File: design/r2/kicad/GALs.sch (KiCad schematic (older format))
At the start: 11 parts, among them IC10 ATF22V10C, IC2 ATF16V8BQL-15PU, IC3 ATF22V10C, IC5 ATF16V8BQL-15PU

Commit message: Tidy up footprints
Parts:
- C10, C12, C30: footprint Capacitor_THT:C_Rect_L4.0mm_W2.5mm_P2.50mm -> rosco_m68k:C2.5-3
- IC2, IC5: footprint rosco_m68k:DIL20 -> Package_DIP:DIP-24_W7.62mm_Socket_LongPads
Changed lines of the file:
@@
 $Descr A4 11693 8268
 encoding utf-8
-Sheet 8 7
+Sheet 7 7
 Title "rosco_m68k Pro (030) Prototype"
 Date "2021-10-01"
@@
 F 0 "C12" H 5910 3715 59  0000 L BNN
 F 1 "100nF" H 5910 3515 59  0000 L BNN
-F 2 "Capacitor_THT:C_Rect_L4.0mm_W2.5mm_P2.50mm" H 5850 3700 50  0001 C CNN
+F 2 "rosco_m68k:C2.5-3" H 5850 3700 50  0001 C CNN
 F 3 "" H 5850 3700 50  0001 C CNN
 	1    5850 3700
@@
 F 0 "C31" H 8060 3715 59  0000 L BNN
 F 1 "100nF" H 8060 3515 59  0000 L BNN
-F 2 "Capacitor_THT:C_Rect_L4.0mm_W2.5mm_P2.50mm" H 8000 3700 50  0001 C CNN
+F 2 "rosco_m68k:C2.5-3" H 8000 3700 50  0001 C CNN
 F 3 "" H 8000 3700 50  0001 C CNN
 	1    8000 3700
@@
 F 0 "IC5" H 6950 4786 59  0000 C CNN
 F 1 "ATF16V8BQL-15PU" H 6950 4681 59  0000 C CNN
-F 2 "rosco_m68k:DIL20" H 6950 3900 50  0001 C CNN
-F 3 "" H 6950 3900 50  0001 C CNN
+F 2 "Package_DIP:DIP-24_W7.62mm_Socket_LongPads" H 6950 3900 50  0001 C CNN
+F 3 "https://www.mouser.com/datasheet/2/268/doc0735-1369018.pdf" H 6950 3900 50  0001 C CNN
 	1    6950 3900
 	1    0    0    -1
@@
 F 0 "IC2" H 2500 4786 59  0000 C CNN
 F 1 "ATF16V8BQL-15PU" H 2500 4681 59  0000 C CNN
-F 2 "rosco_m68k:DIL20" H 2500 3900 50  0001 C CNN
-F 3 "" H 2500 3900 50  0001 C CNN
+F 2 "Package_DIP:DIP-24_W7.62mm_Socket_LongPads" H 2500 3900 50  0001 C CNN
+F 3 "https://www.mouser.com/datasheet/2/268/doc0735-1369018.pdf" H 2500 3900 50  0001 C CNN
 	1    2500 3900
 	1    0    0    -1
@@
 F 0 "C10" H 10360 3715 59  0000 L BNN
 F 1 "100nF" H 10360 3515 59  0000 L BNN
-F 2 "Capacitor_THT:C_Rect_L4.0mm_W2.5mm_P2.50mm" H 10300 3700 50  0001 C CNN
+F 2 "rosco_m68k:C2.5-3" H 10300 3700 50  0001 C CNN
 F 3 "" H 10300 3700 50  0001 C CNN
 	1    10300 3700

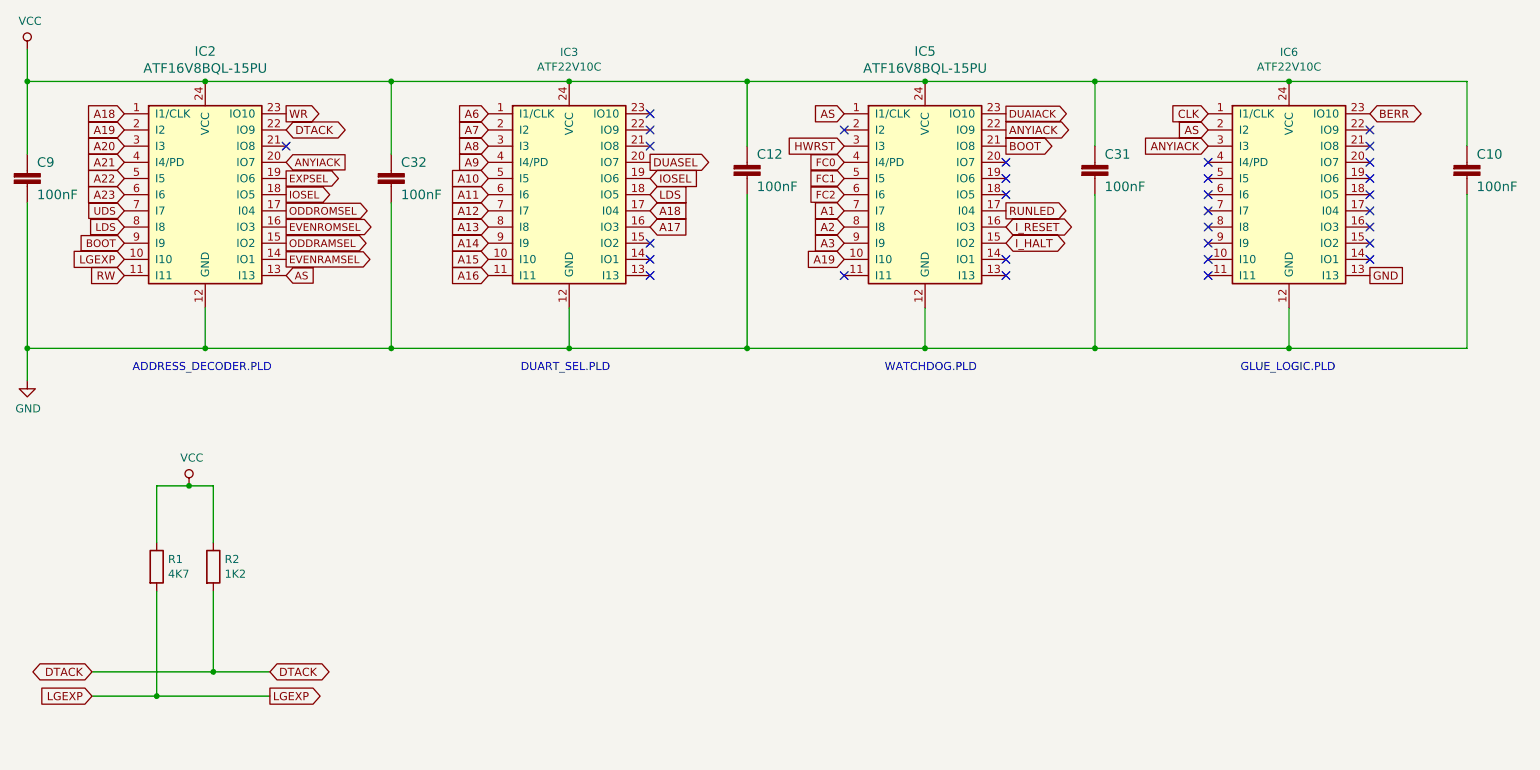
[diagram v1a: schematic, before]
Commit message: Schematic / GAL tweaks and do layout
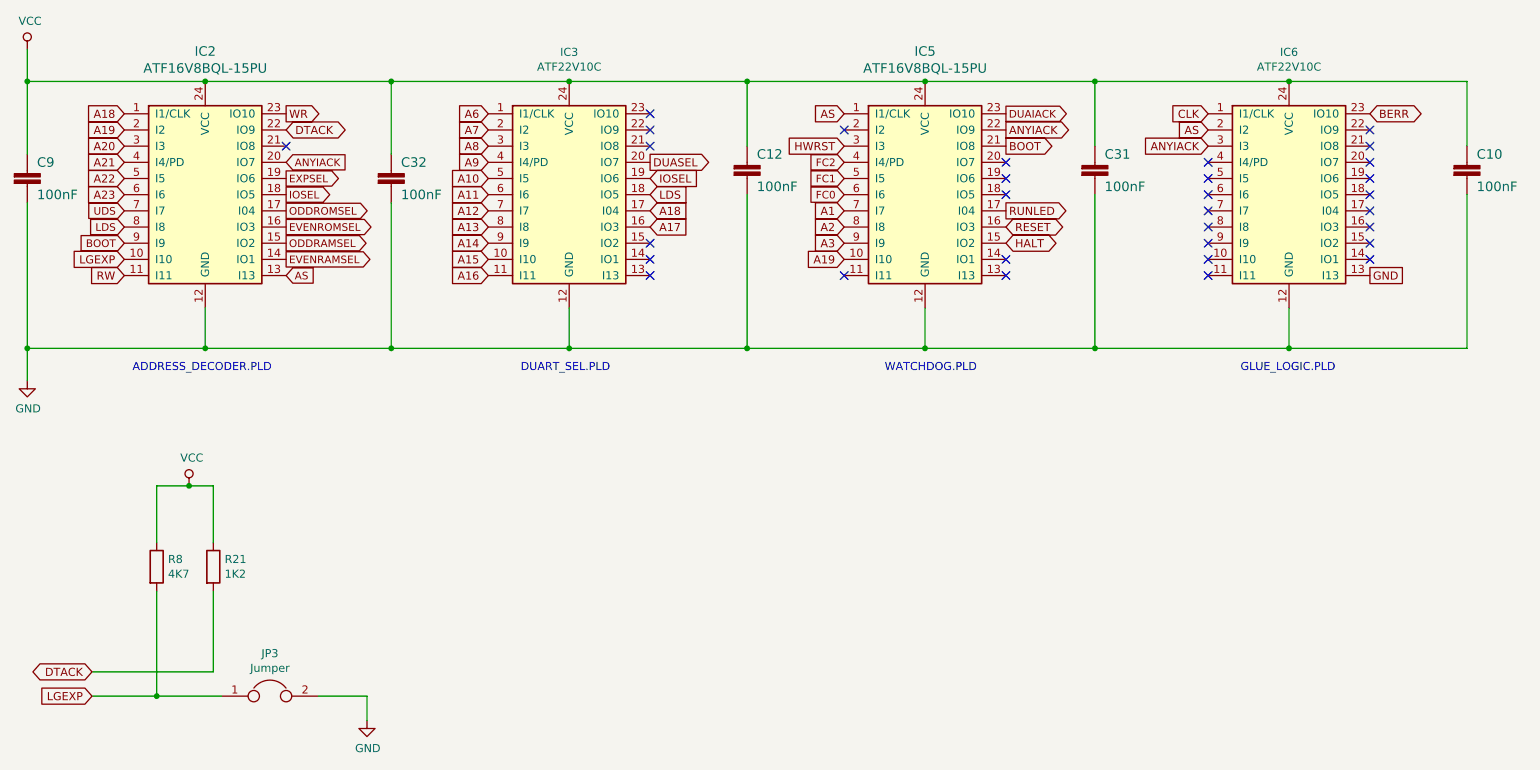
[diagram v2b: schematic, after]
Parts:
- added JP3: Jumper, rosco_m68k:1X02, symbol Device:Jumper
- renumbered R2 to R21, R1 to R8
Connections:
- net FC0: now also IC5.6 (I6); no longer IC5.4 (I4/PD)
- net FC2: now also IC5.4 (I4/PD); no longer IC5.6 (I6)
- net GND: now also JP3.2
- net LGEXP: now also JP3.1
- net I_HALT renamed HALT
- net I_RESET renamed RESET
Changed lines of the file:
@@
 Wire Wire Line
 	8000 3200 8000 3600
-Text GLabel 6450 3700 0    47   Input ~ 0
+Text GLabel 6450 3900 0    47   Input ~ 0
 FC0
 Text GLabel 6450 3800 0    47   Input ~ 0
 FC1
-Text GLabel 6450 3900 0    47   Input ~ 0
+Text GLabel 6450 3700 0    47   Input ~ 0
 FC2
 Text GLabel 7450 3400 2    47   Output ~ 0
@@
 Wire Wire Line
 	1400 3950 1400 4850
-Text GLabel 2900 6850 2    50   BiDi ~ 0
-DTACK
 Text GLabel 1800 6850 0    50   BiDi ~ 0
 DTACK
 Text GLabel 1800 7000 0    50   Input ~ 0
 LGEXP
-Text GLabel 2900 7000 2    50   Output ~ 0
-LGEXP
 Wire Wire Line
 	1800 6850 2550 6850
@@
 	1800 7000 2200 7000
 $Comp
-L Device:R R1
+L Device:R R8
 U 1 1 61653F75
 P 2200 6200
-F 0 "R1" H 2270 6246 50  0000 L CNN
+F 0 "R8" H 2270 6246 50  0000 L CNN
 F 1 "4K7" H 2270 6155 50  0000 L CNN
 F 2 "rosco_m68k:0207_10" V 2130 6200 50  0001 C CNN
@@
 $EndComp
 $Comp
-L Device:R R2
+L Device:R R21
 U 1 1 61654750
 P 2550 6200
-F 0 "R2" H 2620 6246 50  0000 L CNN
+F 0 "R21" H 2620 6246 50  0000 L CNN
 F 1 "1K2" H 2620 6155 50  0000 L CNN
 F 2 "rosco_m68k:0207_10" V 2480 6200 50  0001 C CNN
@@
 Wire Wire Line
 	2200 6350 2200 7000
-Connection ~ 2200 7000
-Wire Wire Line
-	2200 7000 2900 7000
 Wire Wire Line
 	2550 6350 2550 6850
-Connection ~ 2550 6850
-Wire Wire Line
-	2550 6850 2900 6850
 Text GLabel 6450 3600 0    50   Input ~ 0
 HWRST
@@
 RUNLED
 Text GLabel 7450 4100 2    50   3State ~ 0
-I_RESET
+RESET
 Text GLabel 7450 4200 2    50   3State ~ 0
-I_HALT
+HALT
 NoConn ~ 7450 3700
 NoConn ~ 7450 4300
@@
 DUART_SEL.PLD
 NoConn ~ 9700 4100
+$Comp
+L Device:Jumper JP3
+U 1 1 617668AC
+P 2900 7000
+F 0 "JP3" H 2900 7264 50  0000 C CNN
+F 1 "Jumper" H 2900 7173 50  0000 C CNN
+F 2 "rosco_m68k:1X02" H 2900 7000 50  0001 C CNN
+F 3 "~" H 2900 7000 50  0001 C CNN
+	1    2900 7000
+	1    0    0    -1
+$EndComp
+Wire Wire Line
+	2200 7000 2600 7000
+Connection ~ 2200 7000
+$Comp
+L power:GND #PWR?
+U 1 1 61767A5B
+P 3500 7150
+AR Path="/5E53B630/61767A5B" Ref="#PWR?"  Part="1"
+AR Path="/5E53B952/61767A5B" Ref="#PWR?"  Part="1"
+AR Path="/617D19F3/61767A5B" Ref="#PWR05"  Part="1"
+F 0 "#PWR05" H 3500 6900 50  0001 C CNN
+F 1 "GND" H 3505 6977 50  0000 C CNN
+F 2 "" H 3500 7150 50  0001 C CNN
+F 3 "" H 3500 7150 50  0001 C CNN
+	1    3500 7150
+	1    0    0    -1
+$EndComp
+Wire Wire Line
+	3200 7000 3500 7000
+Wire Wire Line
+	3500 7000 3500 7150
 $EndSCHEMATC

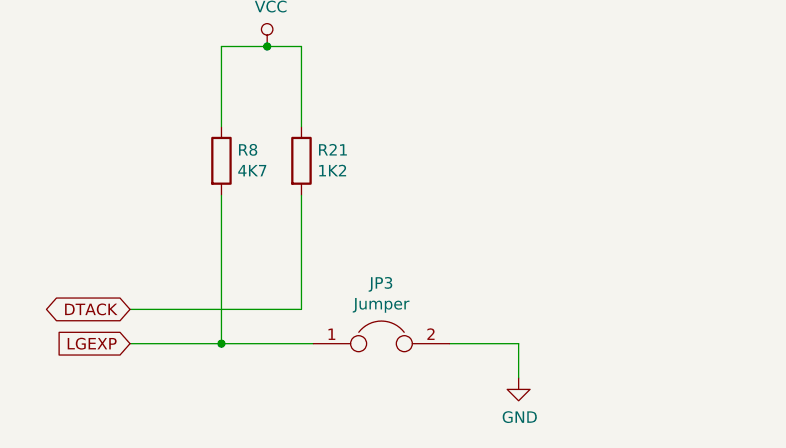
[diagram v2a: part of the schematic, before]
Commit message: Add ROM write-enable jumper and tidy up
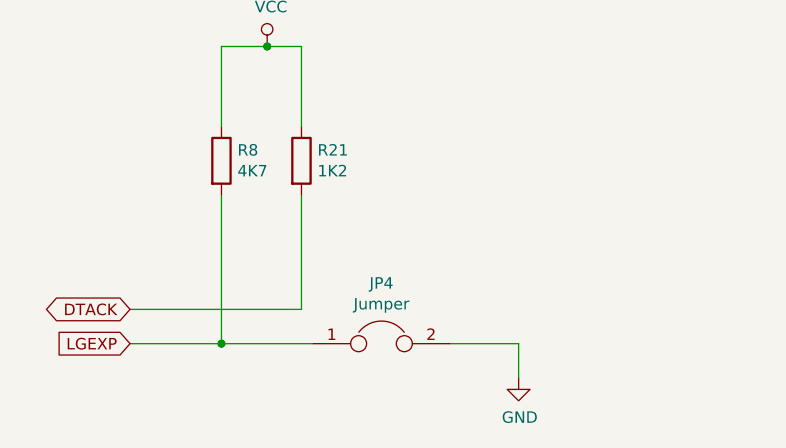
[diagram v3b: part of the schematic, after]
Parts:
- renumbered JP3 to JP4
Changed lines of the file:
@@
 NoConn ~ 9700 4100
 $Comp
-L Device:Jumper JP3
+L Device:Jumper JP4
 U 1 1 617668AC
 P 2900 7000
-F 0 "JP3" H 2900 7264 50  0000 C CNN
+F 0 "JP4" H 2900 7264 50  0000 C CNN
 F 1 "Jumper" H 2900 7173 50  0000 C CNN
 F 2 "rosco_m68k:1X02" H 2900 7000 50  0001 C CNN

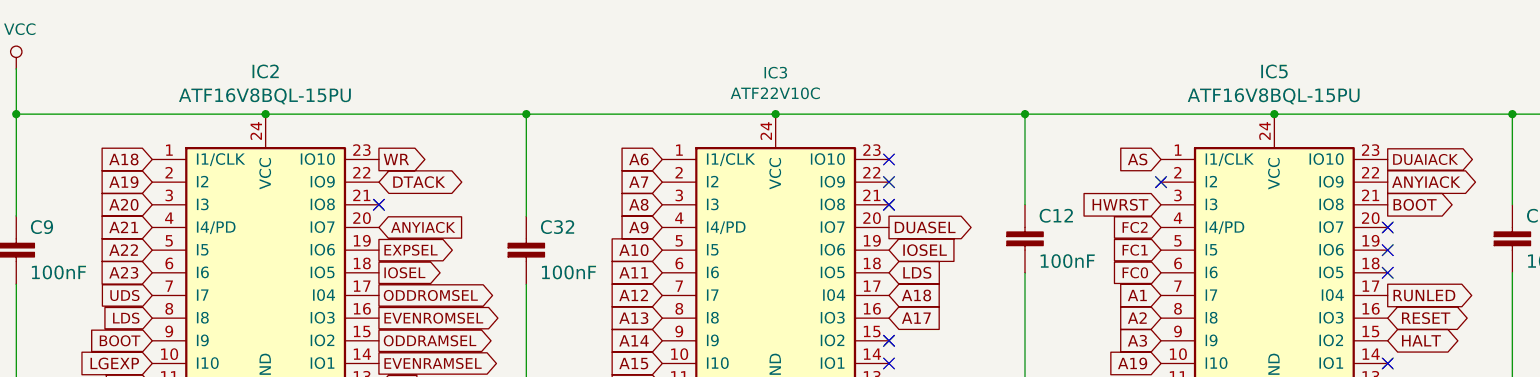
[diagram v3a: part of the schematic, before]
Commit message: Fix incorrect GAL value and redo BOM etc
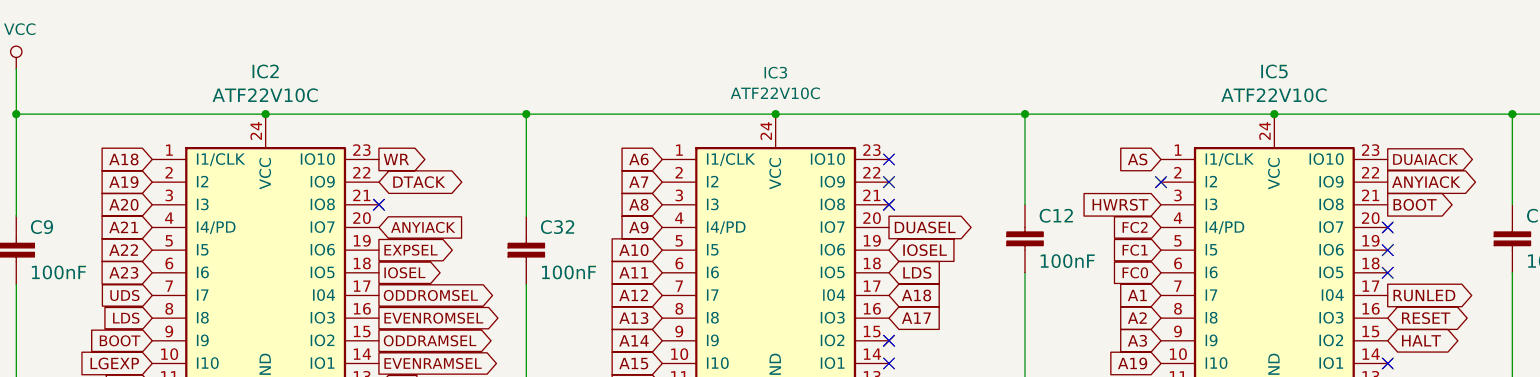
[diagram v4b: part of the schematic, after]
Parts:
- IC2, IC5: value ATF16V8BQL-15PU -> ATF22V10C
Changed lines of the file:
@@
 AR Path="/617D19F3/6161CAA3" Ref="IC5"  Part="1"
 F 0 "IC5" H 6950 4786 59  0000 C CNN
-F 1 "ATF16V8BQL-15PU" H 6950 4681 59  0000 C CNN
+F 1 "ATF22V10C" H 6950 4681 59  0000 C CNN
 F 2 "Package_DIP:DIP-24_W7.62mm_Socket_LongPads" H 6950 3900 50  0001 C CNN
 F 3 "https://www.mouser.com/datasheet/2/268/doc0735-1369018.pdf" H 6950 3900 50  0001 C CNN
@@
 AR Path="/617D19F3/6161CADA" Ref="IC2"  Part="1"
 F 0 "IC2" H 2500 4786 59  0000 C CNN
-F 1 "ATF16V8BQL-15PU" H 2500 4681 59  0000 C CNN
+F 1 "ATF22V10C" H 2500 4681 59  0000 C CNN
 F 2 "Package_DIP:DIP-24_W7.62mm_Socket_LongPads" H 2500 3900 50  0001 C CNN
 F 3 "https://www.mouser.com/datasheet/2/268/doc0735-1369018.pdf" H 2500 3900 50  0001 C CNN

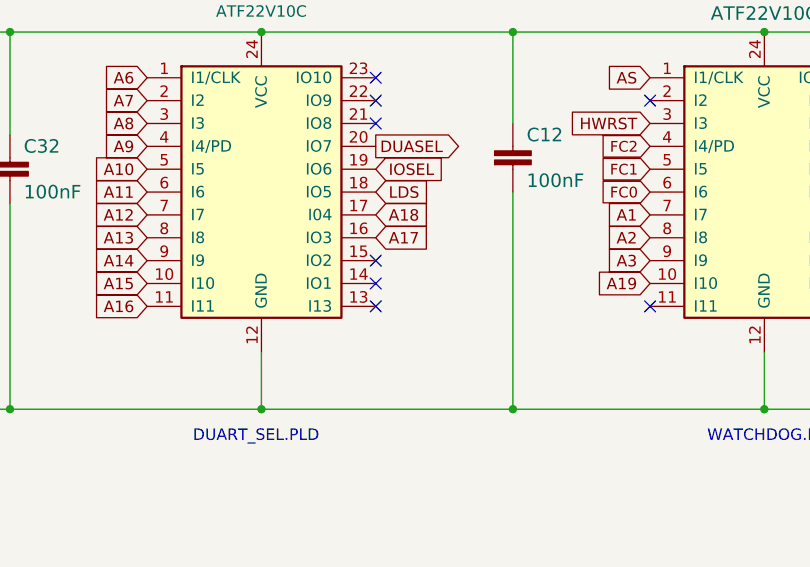
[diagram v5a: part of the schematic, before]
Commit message: Fully decode for DUART
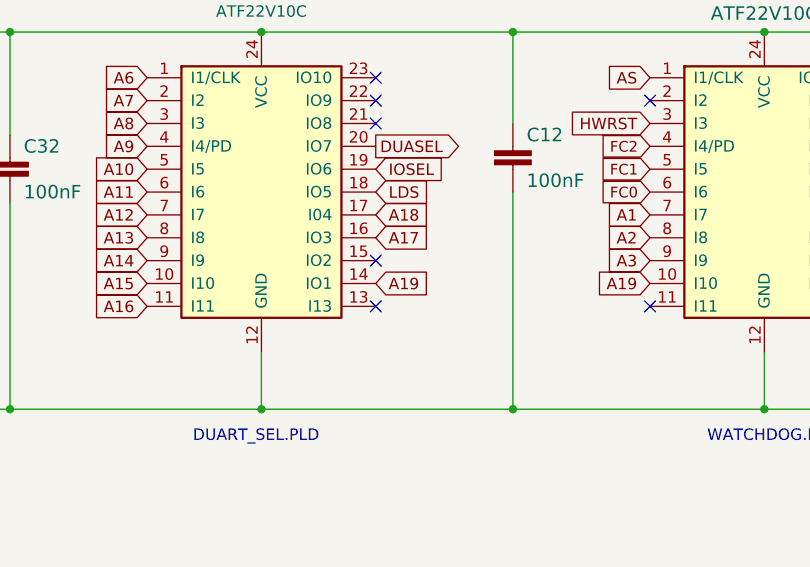
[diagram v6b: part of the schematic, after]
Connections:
- net A19: now also IC3.14 (IO1)
- no-connect marks 31 -> 30
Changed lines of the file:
@@
 NoConn ~ 5250 3400
 NoConn ~ 5250 4200
-NoConn ~ 5250 4300
 NoConn ~ 5250 4400
 Connection ~ 8000 3200
@@
 Wire Wire Line
 	3500 7000 3500 7150
+Text GLabel 5250 4300 2    50   Input ~ 0
+A19
 $EndSCHEMATC
